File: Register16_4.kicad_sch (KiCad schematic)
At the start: 4 parts

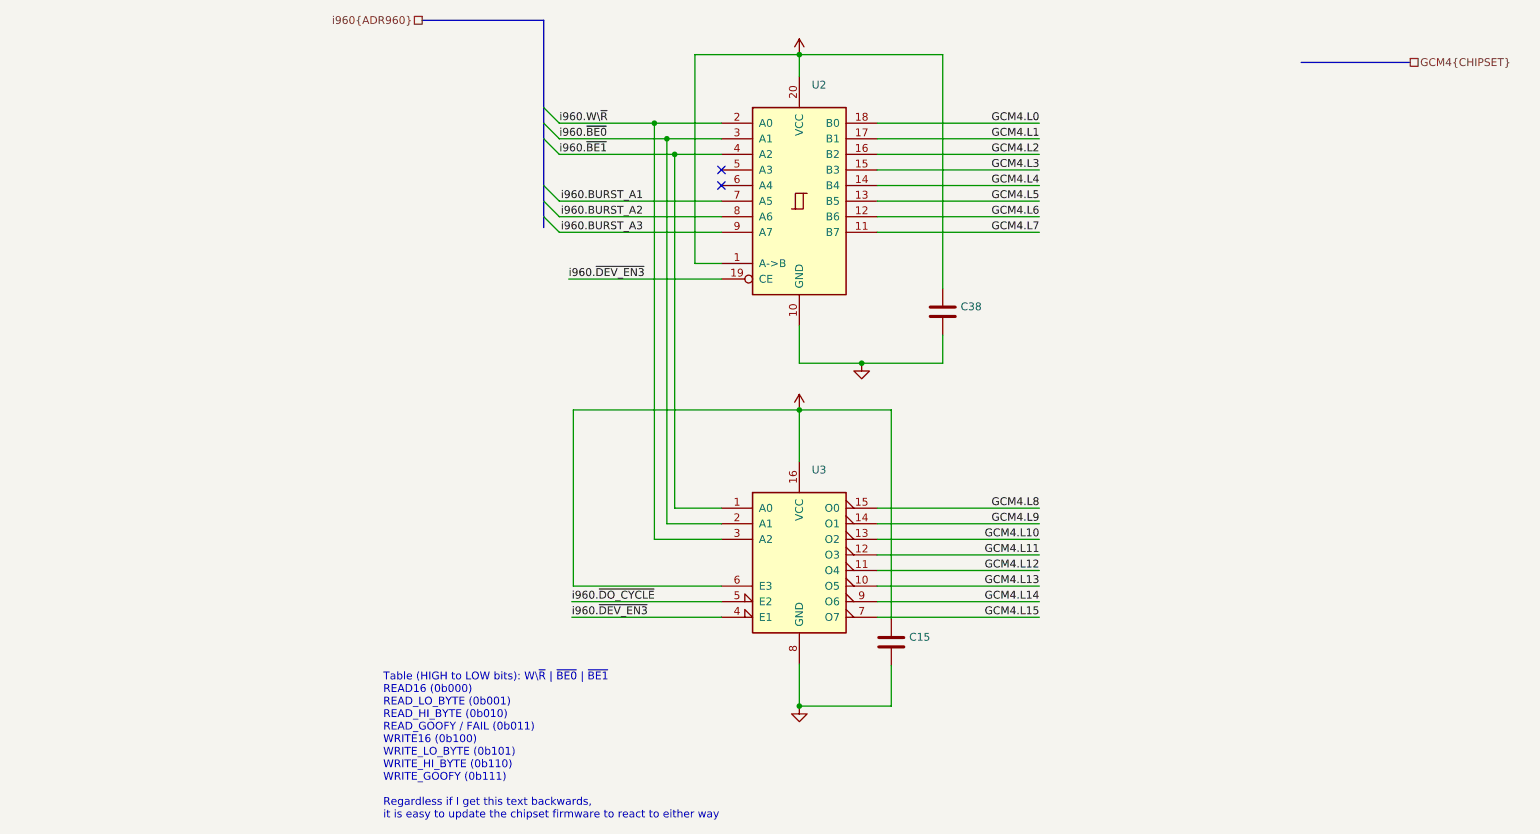
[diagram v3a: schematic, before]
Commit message: Use an AHC245 instead of the 138
We cannot have the hc138 directly connected because it won't be
tristated. Instead use an AHC245 to tristate Register three upper and
expose a pin header that allows the unused 10 pins to be tied into the
chipset regardless of voltage.
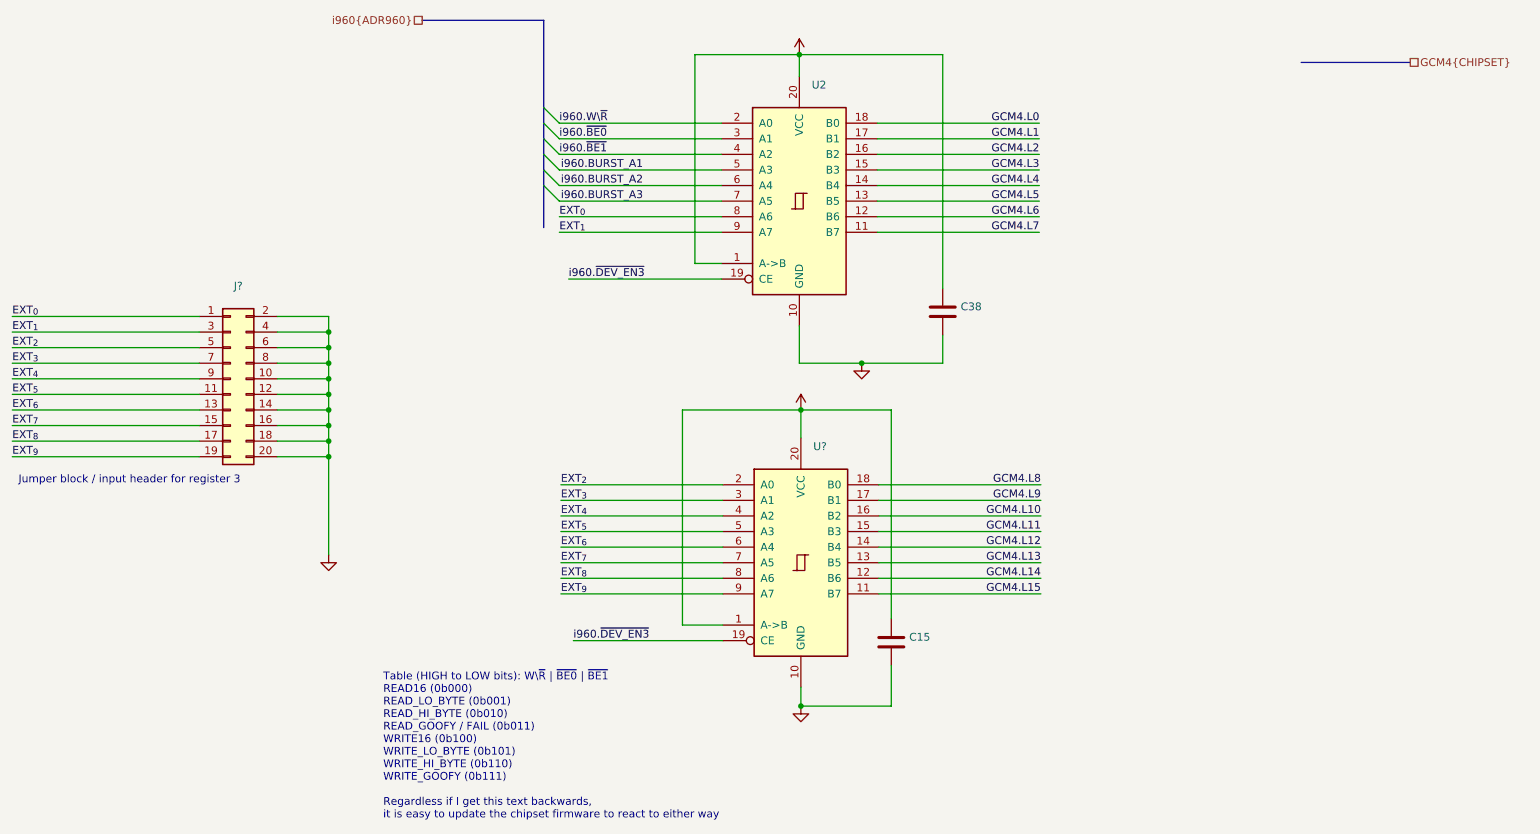
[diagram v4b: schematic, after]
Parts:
- removed U3: (no value), symbol 74xx:74LS138
- added J?: (no value), symbol Connector_Generic:Conn_02x10_Odd_Even
- added U?: (no value), symbol 74xx:74HC245
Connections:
- net GCM4.L10: now also U?.16 (B2)
- net GCM4.L11: now also U?.15 (B3)
- net GCM4.L12: now also U?.14 (B4)
- net GCM4.L13: now also U?.13 (B5)
- net GCM4.L14: now also U?.12 (B6)
- net GCM4.L15: now also U?.11 (B7)
- net GCM4.L8: now also U?.18 (B0)
- net GCM4.L9: now also U?.17 (B1)
- net GND: now also J?.10 (Pin_10), J?.12 (Pin_12), J?.14 (Pin_14), J?.16 (Pin_16), J?.18 (Pin_18), J?.2 (Pin_2), J?.20 (Pin_20), J?.4 (Pin_4), J?.6 (Pin_6), J?.8 (Pin_8), U?.10 (GND)
- net VCC: now also U?.1 (A->B), U?.20 (VCC)
- net i960.BURST_A1: now also U2.5 (A3); no longer U2.7 (A5)
- net i960.BURST_A2: now also U2.6 (A4); no longer U2.8 (A6)
- net i960.BURST_A3: now also U2.7 (A5); no longer U2.9 (A7)
- net i960.~{DEV_EN3}: now also U?.19 (CE)
- new net EXT_{0}: J?.1 (Pin_1), U2.8 (A6)
- new net EXT_{1}: J?.3 (Pin_3), U2.9 (A7)
- new net EXT_{2}: J?.5 (Pin_5), U?.2 (A0)
- new net EXT_{3}: J?.7 (Pin_7), U?.3 (A1)
- new net EXT_{4}: J?.9 (Pin_9), U?.4 (A2)
- new net EXT_{5}: J?.11 (Pin_11), U?.5 (A3)
- new net EXT_{6}: J?.13 (Pin_13), U?.6 (A4)
- new net EXT_{7}: J?.15 (Pin_15), U?.7 (A5)
- new net EXT_{8}: J?.17 (Pin_17), U?.8 (A6)
- new net EXT_{9}: J?.19 (Pin_19), U?.9 (A7)
- no-connect marks 2 -> 0
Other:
- note added: "Jumper block / input header for register 3"

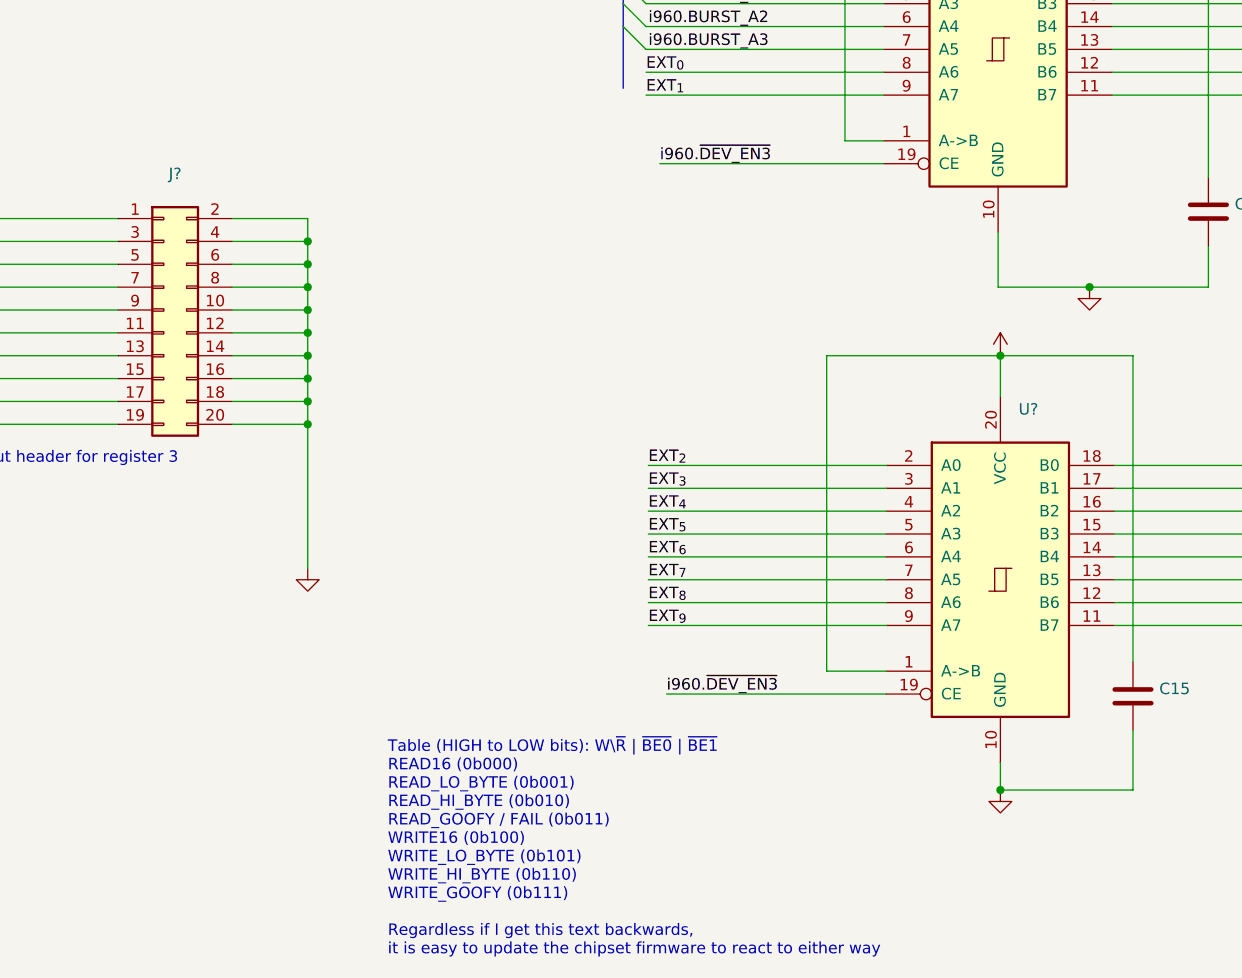
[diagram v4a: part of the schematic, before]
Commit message: Added extra resistor pack for missing pullup part
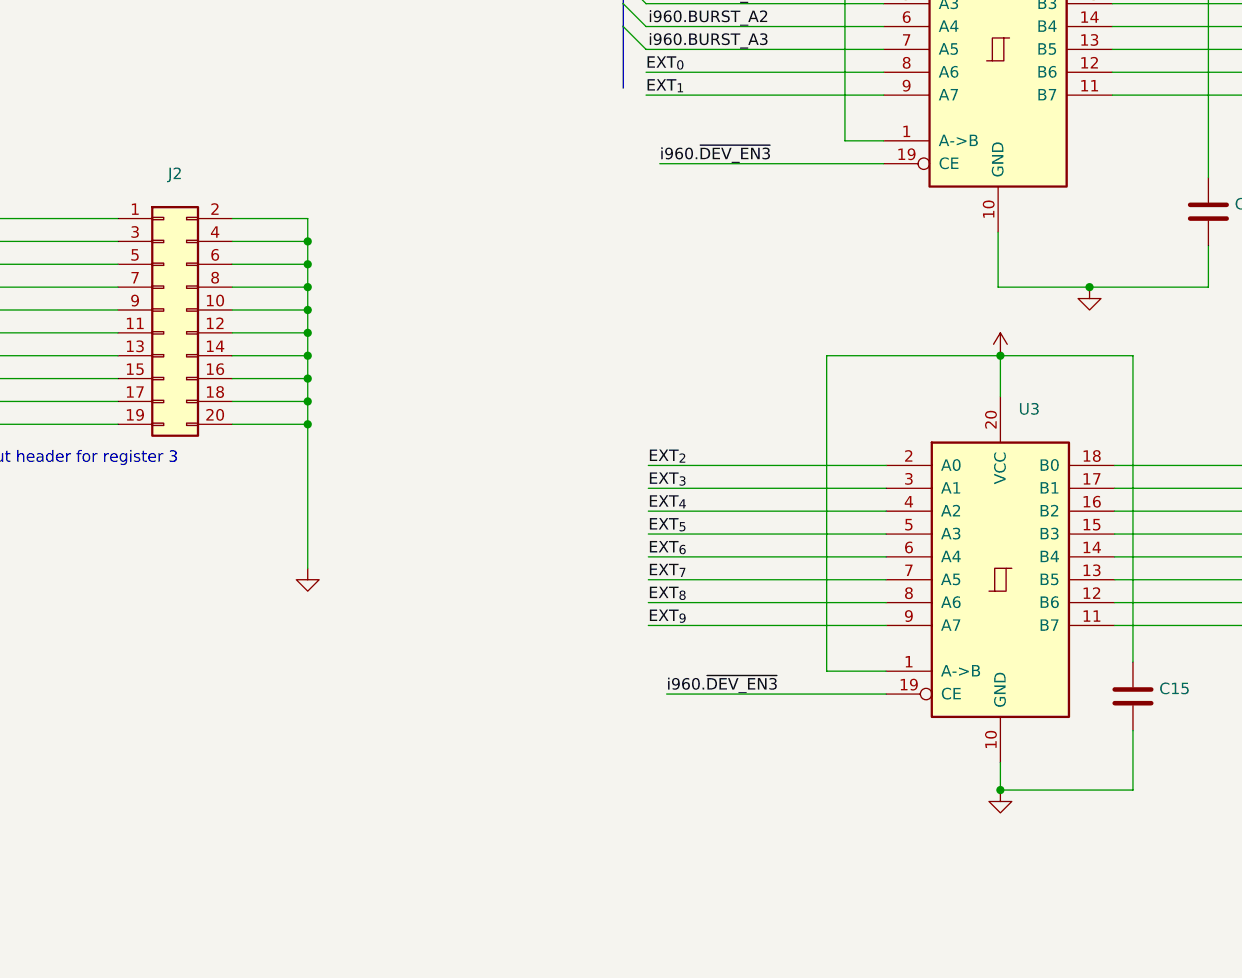
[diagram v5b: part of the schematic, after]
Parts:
- gave numbers to parts that had none: 2
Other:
- note removed: "Table (HIGH to LOW bits): W\~{R} | ~{BE0} | ~{BE1} READ16 (0b000) READ_LO_BYTE (0b001) READ_HI_BYTE (0b010) READ_GOOFY / FAIL (0b011) WRITE16 (0b100) WRITE_LO_BYTE (0b101) WRITE_HI_BYTE (0b110) WRITE_GOOFY (0b111) Regardless if I get this text backwards, it is easy to update the chipset firmware to react to either way"
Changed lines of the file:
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@@
     (stroke (width 0) (type default) (color 0 0 0 0))
-  )
-  (text "Table (HIGH to LOW bits): W\\~{R} | ~{BE0} | ~{BE1}\nREAD16 (0b000)\nREAD_LO_BYTE (0b001)\nREAD_HI_BYTE (0b010)\nREAD_GOOFY / FAIL (0b011)\nWRITE16 (0b100)\nWRITE_LO_BYTE (0b101)\nWRITE_HI_BYTE (0b110)\nWRITE_GOOFY (0b111)\n\nRegardless if I get this text backwards, \nit is easy to update the chipset firmware to react to either way"
-    (at 74.422 153.67 0)
-    (effects (font (size 1.27 1.27)) (justify left bottom))
   )
   (text "Jumper block / input header for register 3" (at 14.986 99.06 0)
@@
   (symbol (lib_id "power:GND") (at 65.532 110.49 0) (unit 1)
     (in_bom yes) (on_board yes) (fields_autoplaced)
-    (property "Reference" "#PWR?" (id 0) (at 65.532 116.84 0)
+    (property "Reference" "#PWR024" (id 0) (at 65.532 116.84 0)
       (effects (font (size 1.27 1.27)) hide)
     )
@@
   (symbol (lib_id "74xx:74HC245") (at 142.494 111.76 0) (unit 1)
     (in_bom yes) (on_board yes) (fields_autoplaced)
-    (property "Reference" "U?" (id 0) (at 144.5134 92.8202 0)
+    (property "Reference" "U3" (id 0) (at 144.5134 92.8202 0)
       (effects (font (size 1.27 1.27)) (justify left))
     )
@@
   (symbol (lib_id "Connector_Generic:Conn_02x10_Odd_Even") (at 49.53 81.788 0) (unit 1)
     (in_bom yes) (on_board yes) (fields_autoplaced)
-    (property "Reference" "J?" (id 0) (at 50.8 66.6582 0))
+    (property "Reference" "J2" (id 0) (at 50.8 66.6582 0))
     (property "Value" "" (id 1) (at 50.8 69.1951 0))
     (property "Footprint" "" (id 2) (at 49.53 81.788 0)

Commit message: Flatten the design so that address lines are dedicated 16 like data
It needs to be as simple as possible regardless. I don't need extra
chips to foul things up
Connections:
- net i960.W\~{R} is gone; now on net i960.~{BE0}: U2.2 (A0)
- net EXT_{0}: now also J2.19 (Pin_19), U2.7 (A5); no longer J2.1 (Pin_1), U2.8 (A6)
- net EXT_{1}: now also J2.17 (Pin_17), U2.8 (A6); no longer J2.3 (Pin_3), U2.9 (A7)
- net EXT_{2}: now also J2.15 (Pin_15), U2.9 (A7); no longer J2.5 (Pin_5), U3.2 (A0)
- net EXT_{3}: now also J2.13 (Pin_13), U3.2 (A0); no longer J2.7 (Pin_7), U3.3 (A1)
- net EXT_{4}: now also J2.11 (Pin_11), U3.3 (A1); no longer J2.9 (Pin_9), U3.4 (A2)
- net EXT_{5}: now also J2.9 (Pin_9), U3.4 (A2); no longer J2.11 (Pin_11), U3.5 (A3)
- net EXT_{6}: now also J2.7 (Pin_7), U3.5 (A3); no longer J2.13 (Pin_13), U3.6 (A4)
- net EXT_{7}: now also J2.5 (Pin_5), U3.6 (A4); no longer J2.15 (Pin_15), U3.7 (A5)
- net EXT_{8}: now also J2.3 (Pin_3), U3.7 (A5); no longer J2.17 (Pin_17), U3.8 (A6)
- net EXT_{9}: now also J2.1 (Pin_1), U3.8 (A6); no longer J2.19 (Pin_19), U3.9 (A7)
- net i960.BURST_A1: now also U2.4 (A2); no longer U2.5 (A3)
- net i960.BURST_A2: now also U2.5 (A3); no longer U2.6 (A4)
- net i960.BURST_A3: now also U2.6 (A4); no longer U2.7 (A5)
- net i960.~{BE0}: no longer U2.3 (A1)
- net i960.~{BE1}: now also U2.3 (A1); no longer U2.4 (A2)
- new net EXT_{10}: U3.9 (A7)
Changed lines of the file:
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@@
     (effects (font (size 1.27 1.27)) (justify right bottom))
   )
-  (label "EXT_{4}" (at 103.378 104.14 0)
+  (label "EXT_{4}" (at 103.378 101.6 0)
     (effects (font (size 1.27 1.27)) (justify left bottom))
   )
-  (label "EXT_{2}" (at 103.378 99.06 0)
+  (label "EXT_{2}" (at 103.124 57.912 0)
     (effects (font (size 1.27 1.27)) (justify left bottom))
   )
-  (label "i960.~{BE0}" (at 103.124 42.672 0)
+  (label "i960.~{BE0}" (at 103.124 40.132 0)
     (effects (font (size 1.27 1.27)) (justify left bottom))
   )
-  (label "EXT_{1}" (at 103.124 57.912 0)
+  (label "EXT_{1}" (at 103.124 55.372 0)
     (effects (font (size 1.27 1.27)) (justify left bottom))
   )
@@
     (effects (font (size 1.27 1.27)) (justify right bottom))
   )
-  (label "EXT_{1}" (at 13.97 74.168 0)
+  (label "EXT_{1}" (at 13.97 91.948 0)
     (effects (font (size 1.27 1.27)) (justify left bottom))
   )
@@
     (effects (font (size 1.27 1.27)) (justify left bottom))
   )
-  (label "EXT_{8}" (at 13.97 91.948 0)
+  (label "EXT_{8}" (at 13.97 74.168 0)
     (effects (font (size 1.27 1.27)) (justify left bottom))
   )
-  (label "EXT_{7}" (at 103.378 111.76 0)
+  (label "EXT_{7}" (at 103.378 109.22 0)
     (effects (font (size 1.27 1.27)) (justify left bottom))
   )
-  (label "i960.BURST_A1" (at 103.378 47.752 0)
+  (label "i960.BURST_A1" (at 103.378 45.212 0)
     (effects (font (size 1.27 1.27)) (justify left bottom))
   )
@@
     (effects (font (size 1.27 1.27)) (justify right bottom))
   )
-  (label "EXT_{3}" (at 13.97 79.248 0)
+  (label "EXT_{3}" (at 13.97 86.868 0)
     (effects (font (size 1.27 1.27)) (justify left bottom))
   )
-  (label "i960.BURST_A2" (at 103.378 50.292 0)
+  (label "i960.BURST_A2" (at 103.378 47.752 0)
     (effects (font (size 1.27 1.27)) (justify left bottom))
   )
@@
     (effects (font (size 1.27 1.27)) (justify right bottom))
   )
-  (label "EXT_{0}" (at 13.97 71.628 0)
+  (label "EXT_{0}" (at 13.97 94.488 0)
     (effects (font (size 1.27 1.27)) (justify left bottom))
   )
-  (label "EXT_{9}" (at 103.378 116.84 0)
+  (label "EXT_{9}" (at 103.378 114.3 0)
+    (effects (font (size 1.27 1.27)) (justify left bottom))
+  )
+  (label "EXT_{10}" (at 103.378 116.84 0)
     (effects (font (size 1.27 1.27)) (justify left bottom))
   )
@@
     (effects (font (size 1.27 1.27)) (justify left bottom))
   )
-  (label "EXT_{6}" (at 13.97 86.868 0)
+  (label "EXT_{6}" (at 13.97 79.248 0)
     (effects (font (size 1.27 1.27)) (justify left bottom))
   )
@@
     (effects (font (size 1.27 1.27)) (justify right bottom))
   )
-  (label "EXT_{0}" (at 103.124 55.372 0)
+  (label "EXT_{0}" (at 103.124 52.832 0)
     (effects (font (size 1.27 1.27)) (justify left bottom))
   )
@@
     (effects (font (size 1.27 1.27)) (justify right bottom))
   )
-  (label "EXT_{5}" (at 103.378 106.68 0)
+  (label "EXT_{5}" (at 103.378 104.14 0)
     (effects (font (size 1.27 1.27)) (justify left bottom))
   )
-  (label "EXT_{2}" (at 13.97 76.708 0)
+  (label "EXT_{2}" (at 13.97 89.408 0)
     (effects (font (size 1.27 1.27)) (justify left bottom))
   )
@@
     (effects (font (size 1.27 1.27)) (justify right bottom))
   )
-  (label "EXT_{9}" (at 13.97 94.488 0)
+  (label "EXT_{9}" (at 13.97 71.628 0)
     (effects (font (size 1.27 1.27)) (justify left bottom))
   )
-  (label "i960.BURST_A3" (at 103.378 52.832 0)
+  (label "i960.BURST_A3" (at 103.378 50.292 0)
     (effects (font (size 1.27 1.27)) (justify left bottom))
   )
-  (label "EXT_{6}" (at 103.378 109.22 0)
+  (label "EXT_{6}" (at 103.378 106.68 0)
     (effects (font (size 1.27 1.27)) (justify left bottom))
   )
-  (label "EXT_{5}" (at 13.97 84.328 0)
+  (label "EXT_{5}" (at 13.97 81.788 0)
     (effects (font (size 1.27 1.27)) (justify left bottom))
   )
@@
     (effects (font (size 1.27 1.27)) (justify right bottom))
   )
-  (label "EXT_{8}" (at 103.378 114.3 0)
+  (label "EXT_{8}" (at 103.378 111.76 0)
     (effects (font (size 1.27 1.27)) (justify left bottom))
   )
-  (label "EXT_{4}" (at 13.97 81.788 0)
+  (label "EXT_{4}" (at 13.97 84.328 0)
     (effects (font (size 1.27 1.27)) (justify left bottom))
   )
-  (label "i960.W\\~{R}" (at 103.124 40.132 0)
-    (effects (font (size 1.27 1.27)) (justify left bottom))
-  )
-  (label "EXT_{7}" (at 13.97 89.408 0)
+  (label "EXT_{7}" (at 13.97 76.708 0)
     (effects (font (size 1.27 1.27)) (justify left bottom))
   )
@@
     (effects (font (size 1.27 1.27)) (justify right bottom))
   )
-  (label "EXT_{3}" (at 103.378 101.6 0)
+  (label "EXT_{3}" (at 103.378 99.06 0)
     (effects (font (size 1.27 1.27)) (justify left bottom))
   )
-  (label "i960.~{BE1}" (at 103.124 45.212 0)
+  (label "i960.~{BE1}" (at 103.124 42.672 0)
     (effects (font (size 1.27 1.27)) (justify left bottom))
   )
